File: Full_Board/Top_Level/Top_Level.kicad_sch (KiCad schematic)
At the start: 4 parts, among them J1 OQ0432500000G, J2 OQ0432500000G, J3 OQ0432500000G, J4 OQ0432500000G

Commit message: Fixed entire BOM for all components
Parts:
- J1, J2, J3, J4: Digikey Link https://www.digikey.com/en/products/detail/amphenol-anytek/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 -> (none); Digikey link (none) -> https://www.digikey.com/en/products/detail/amphenol-anytek/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; Manufacturer's Part Number (none) -> OQ0432500000G; Manufacturer_Part_Number OQ0432500000G -> (none); Mouser Price/Stock https://www.mouser.co.uk/ProductDetail/Amphenol-Anytek/OQ04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 -> (none); Mouser link (none) -> https://www.mouser.com/ProductDetail/Amphenol-Anytek/OQ0432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
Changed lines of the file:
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@@
     (company "The Great Gambit")
-  )
-  (bus_entry (at 72.39 186.69) (size 2.54 2.54)
-    (stroke (width 0) (type default) (color 0 0 0 0))
   )
   (wire (pts (xy 68.58 95.25) (xy 68.58 105.41))
@@
       (effects (font (size 1.27 1.27)) (justify left) hide)
     )
-    (property "Mouser Price/Stock" "https://www.mouser.co.uk/ProductDetail/Amphenol-Anytek/OQ0432500000G?qs=Mv7BduZupUhaPicvo3xrhg%3D%3D" (id 7) (at 140.97 109.22 0)
+    (property "Mouser Price/Stock" "" (id 7) (at 140.97 109.22 0)
       (effects (font (size 1.27 1.27)) (justify left) hide)
     )
@@
       (effects (font (size 1.27 1.27)) (justify left) hide)
     )
-    (property "Manufacturer_Part_Number" "OQ0432500000G" (id 9) (at 140.97 114.3 0)
+    (property "Manufacturer_Part_Number" "" (id 9) (at 140.97 114.3 0)
       (effects (font (size 1.27 1.27)) (justify left) hide)
     )
@@
       (effects (font (size 1.27 1.27)) hide)
     )
-    (property "Digikey Link" "https://www.digikey.com/en/products/detail/amphenol-anytek/OQ0432500000G/2261265" (id 11) (at 157.48 99.06 0)
+    (property "Digikey Link" "" (id 11) (at 157.48 99.06 0)
       (effects (font (size 1.27 1.27)) hide)
     )
     (property "Mouser Link" "" (id 12) (at 157.48 99.06 0)
+      (effects (font (size 1.27 1.27)) hide)
+    )
+    (property "Digikey link" "https://www.digikey.com/en/products/detail/amphenol-anytek/OQ0432500000G/2261265" (id 13) (at 157.48 99.06 0)
+      (effects (font (size 1.27 1.27)) hide)
+    )
+    (property "Manufacturer's Part Number" "OQ0432500000G" (id 14) (at 157.48 99.06 0)
+      (effects (font (size 1.27 1.27)) hide)
+    )
+    (property "Mouser link" "https://www.mouser.com/ProductDetail/Amphenol-Anytek/OQ0432500000G?qs=Mv7BduZupUhaPicvo3xrhg%3D%3D" (id 15) (at 157.48 99.06 0)
       (effects (font (size 1.27 1.27)) hide)
     )
@@
       (effects (font (size 1.27 1.27)) (justify left) hide)
     )
-    (property "Mouser Price/Stock" "https://www.mouser.co.uk/ProductDetail/Amphenol-Anytek/OQ0432500000G?qs=Mv7BduZupUhaPicvo3xrhg%3D%3D" (id 7) (at 273.05 121.92 0)
+    (property "Mouser Price/Stock" "" (id 7) (at 273.05 121.92 0)
       (effects (font (size 1.27 1.27)) (justify left) hide)
     )
@@
       (effects (font (size 1.27 1.27)) (justify left) hide)
     )
-    (property "Manufacturer_Part_Number" "OQ0432500000G" (id 9) (at 273.05 127 0)
+    (property "Manufacturer_Part_Number" "" (id 9) (at 273.05 127 0)
       (effects (font (size 1.27 1.27)) (justify left) hide)
     )
@@
       (effects (font (size 1.27 1.27)) hide)
     )
-    (property "Digikey Link" "https://www.digikey.com/en/products/detail/amphenol-anytek/OQ0432500000G/2261265" (id 11) (at 256.54 111.76 0)
+    (property "Digikey Link" "" (id 11) (at 256.54 111.76 0)
       (effects (font (size 1.27 1.27)) hide)
     )
     (property "Mouser Link" "" (id 12) (at 256.54 111.76 0)
+      (effects (font (size 1.27 1.27)) hide)
+    )
+    (property "Digikey link" "https://www.digikey.com/en/products/detail/amphenol-anytek/OQ0432500000G/2261265" (id 13) (at 256.54 111.76 0)
+      (effects (font (size 1.27 1.27)) hide)
+    )
+    (property "Manufacturer's Part Number" "OQ0432500000G" (id 14) (at 256.54 111.76 0)
+      (effects (font (size 1.27 1.27)) hide)
+    )
+    (property "Mouser link" "https://www.mouser.com/ProductDetail/Amphenol-Anytek/OQ0432500000G?qs=Mv7BduZupUhaPicvo3xrhg%3D%3D" (id 15) (at 256.54 111.76 0)
       (effects (font (size 1.27 1.27)) hide)
     )
@@
       (effects (font (size 1.27 1.27)) (justify left) hide)
     )
-    (property "Mouser Price/Stock" "https://www.mouser.co.uk/ProductDetail/Amphenol-Anytek/OQ0432500000G?qs=Mv7BduZupUhaPicvo3xrhg%3D%3D" (id 7) (at 273.05 59.69 0)
+    (property "Mouser Price/Stock" "" (id 7) (at 273.05 59.69 0)
       (effects (font (size 1.27 1.27)) (justify left) hide)
     )
@@
       (effects (font (size 1.27 1.27)) (justify left) hide)
     )
-    (property "Manufacturer_Part_Number" "OQ0432500000G" (id 9) (at 273.05 64.77 0)
+    (property "Manufacturer_Part_Number" "" (id 9) (at 273.05 64.77 0)
       (effects (font (size 1.27 1.27)) (justify left) hide)
     )
@@
       (effects (font (size 1.27 1.27)) hide)
     )
-    (property "Digikey Link" "https://www.digikey.com/en/products/detail/amphenol-anytek/OQ0432500000G/2261265" (id 11) (at 256.54 49.53 0)
+    (property "Digikey Link" "" (id 11) (at 256.54 49.53 0)
       (effects (font (size 1.27 1.27)) hide)
     )
     (property "Mouser Link" "" (id 12) (at 256.54 49.53 0)
+      (effects (font (size 1.27 1.27)) hide)
+    )
+    (property "Digikey link" "https://www.digikey.com/en/products/detail/amphenol-anytek/OQ0432500000G/2261265" (id 13) (at 256.54 49.53 0)
+      (effects (font (size 1.27 1.27)) hide)
+    )
+    (property "Manufacturer's Part Number" "OQ0432500000G" (id 14) (at 256.54 49.53 0)
+      (effects (font (size 1.27 1.27)) hide)
+    )
+    (property "Mouser link" "https://www.mouser.com/ProductDetail/Amphenol-Anytek/OQ0432500000G?qs=Mv7BduZupUhaPicvo3xrhg%3D%3D" (id 15) (at 256.54 49.53 0)
       (effects (font (size 1.27 1.27)) hide)
     )
@@
       (effects (font (size 1.27 1.27)) (justify left) hide)
     )
-    (property "Mouser Price/Stock" "https://www.mouser.co.uk/ProductDetail/Amphenol-Anytek/OQ0432500000G?qs=Mv7BduZupUhaPicvo3xrhg%3D%3D" (id 7) (at 273.05 90.17 0)
+    (property "Mouser Price/Stock" "" (id 7) (at 273.05 90.17 0)
       (effects (font (size 1.27 1.27)) (justify left) hide)
     )
@@
       (effects (font (size 1.27 1.27)) (justify left) hide)
     )
-    (property "Manufacturer_Part_Number" "OQ0432500000G" (id 9) (at 273.05 95.25 0)
+    (property "Manufacturer_Part_Number" "" (id 9) (at 273.05 95.25 0)
       (effects (font (size 1.27 1.27)) (justify left) hide)
     )
@@
       (effects (font (size 1.27 1.27)) hide)
     )
-    (property "Digikey Link" "https://www.digikey.com/en/products/detail/amphenol-anytek/OQ0432500000G/2261265" (id 11) (at 256.54 80.01 0)
+    (property "Digikey Link" "" (id 11) (at 256.54 80.01 0)
       (effects (font (size 1.27 1.27)) hide)
     )
@@
       (effects (font (size 1.27 1.27)) hide)
     )
+    (property "Digikey link" "https://www.digikey.com/en/products/detail/amphenol-anytek/OQ0432500000G/2261265" (id 13) (at 256.54 80.01 0)
+      (effects (font (size 1.27 1.27)) hide)
+    )
+    (property "Manufacturer's Part Number" "OQ0432500000G" (id 14) (at 256.54 80.01 0)
+      (effects (font (size 1.27 1.27)) hide)
+    )
+    (property "Mouser link" "https://www.mouser.com/ProductDetail/Amphenol-Anytek/OQ0432500000G?qs=Mv7BduZupUhaPicvo3xrhg%3D%3D" (id 15) (at 256.54 80.01 0)
+      (effects (font (size 1.27 1.27)) hide)
+    )

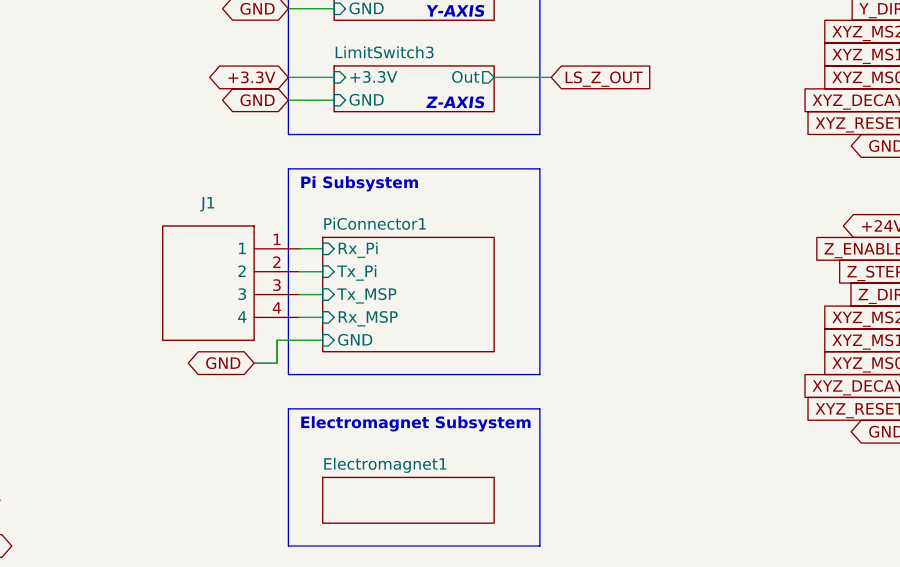
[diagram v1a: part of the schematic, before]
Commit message: Adjusted the Pi subsystem
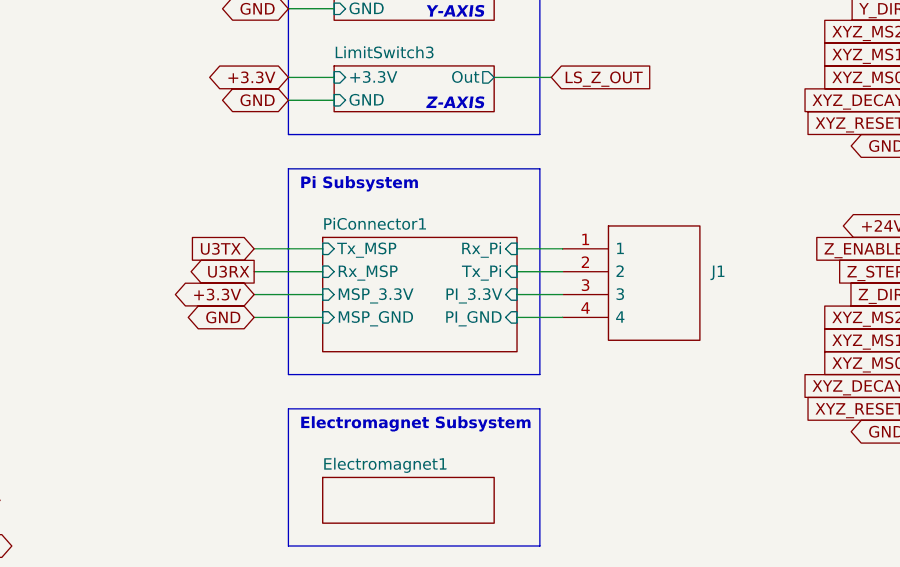
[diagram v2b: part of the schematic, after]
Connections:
- net PiConnector1/Rx_MSP renamed PiConnector1/PI_GND
- net PiConnector1/Tx_MSP renamed PiConnector1/PI_3.3V
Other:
- sheet PiConnector1 ports: added MSP_3.3V, MSP_GND, PI_3.3V, PI_GND; removed GND

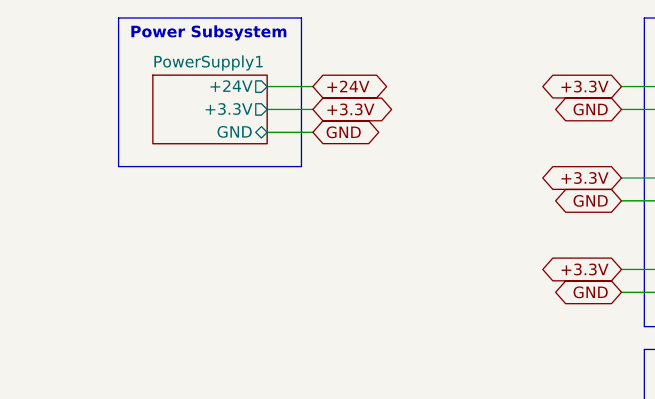
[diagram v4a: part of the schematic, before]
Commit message: Added extra bypass caps to the power supply
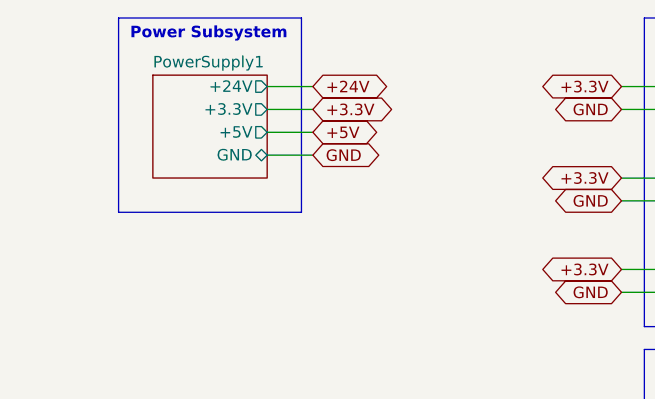
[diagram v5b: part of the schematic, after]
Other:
- sheet PowerSupply1 ports: added +5V; removed none

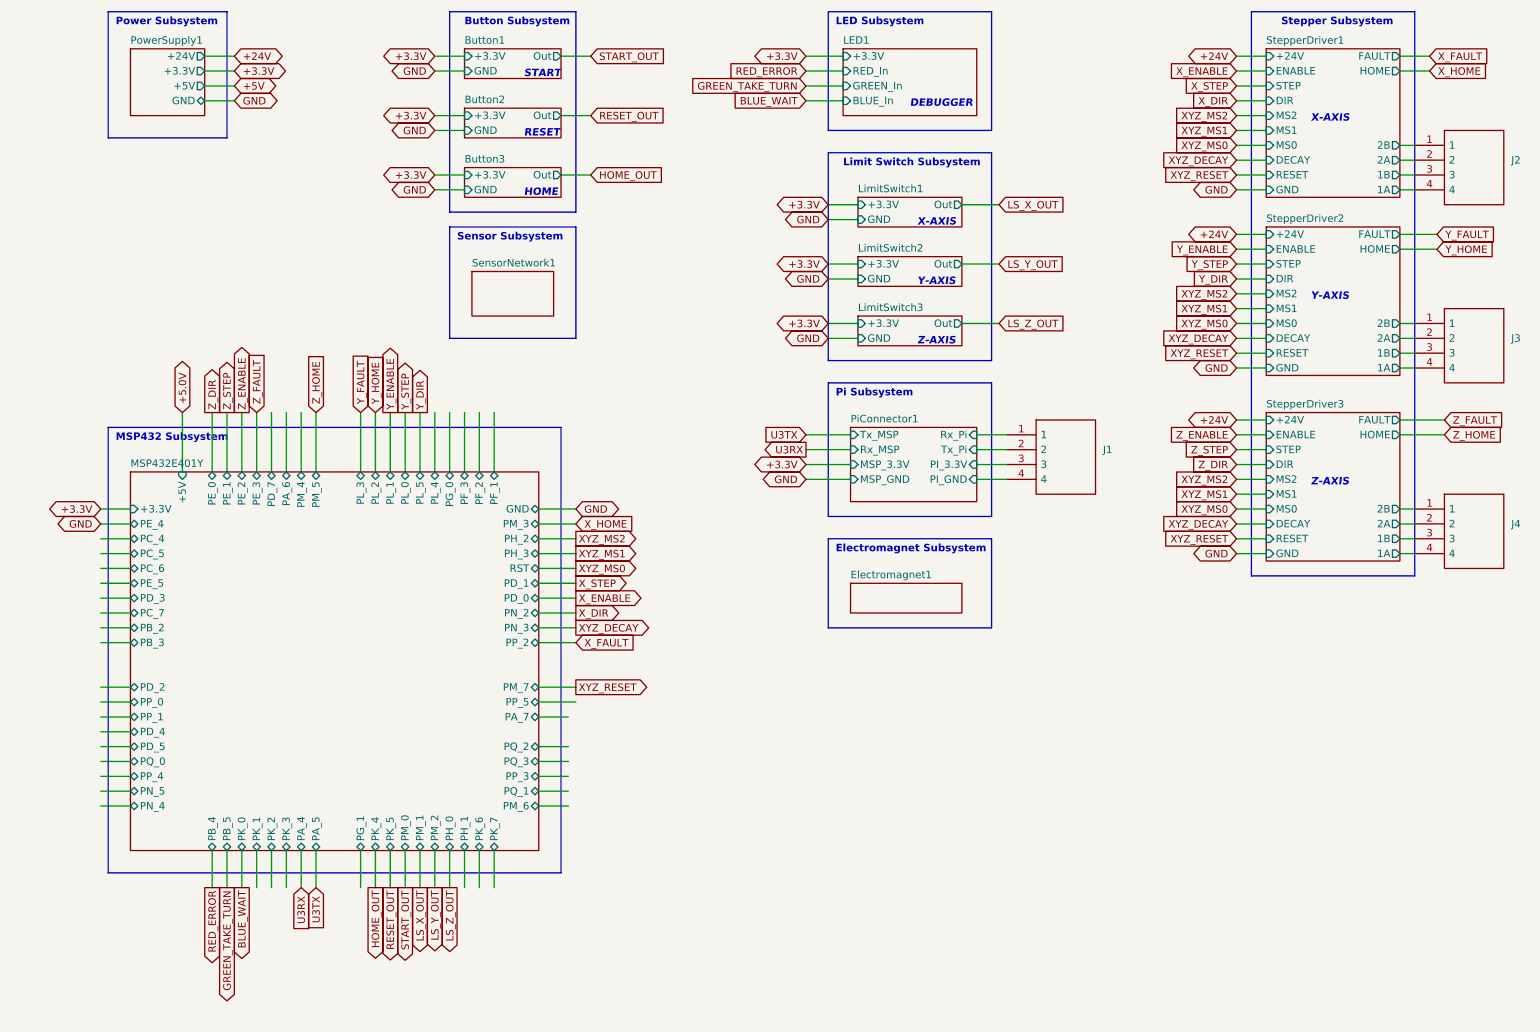
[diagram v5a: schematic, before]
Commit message: Merge Eli and Gabi files. Remove unecessary ECAD remnants. Update stepper components post-part order
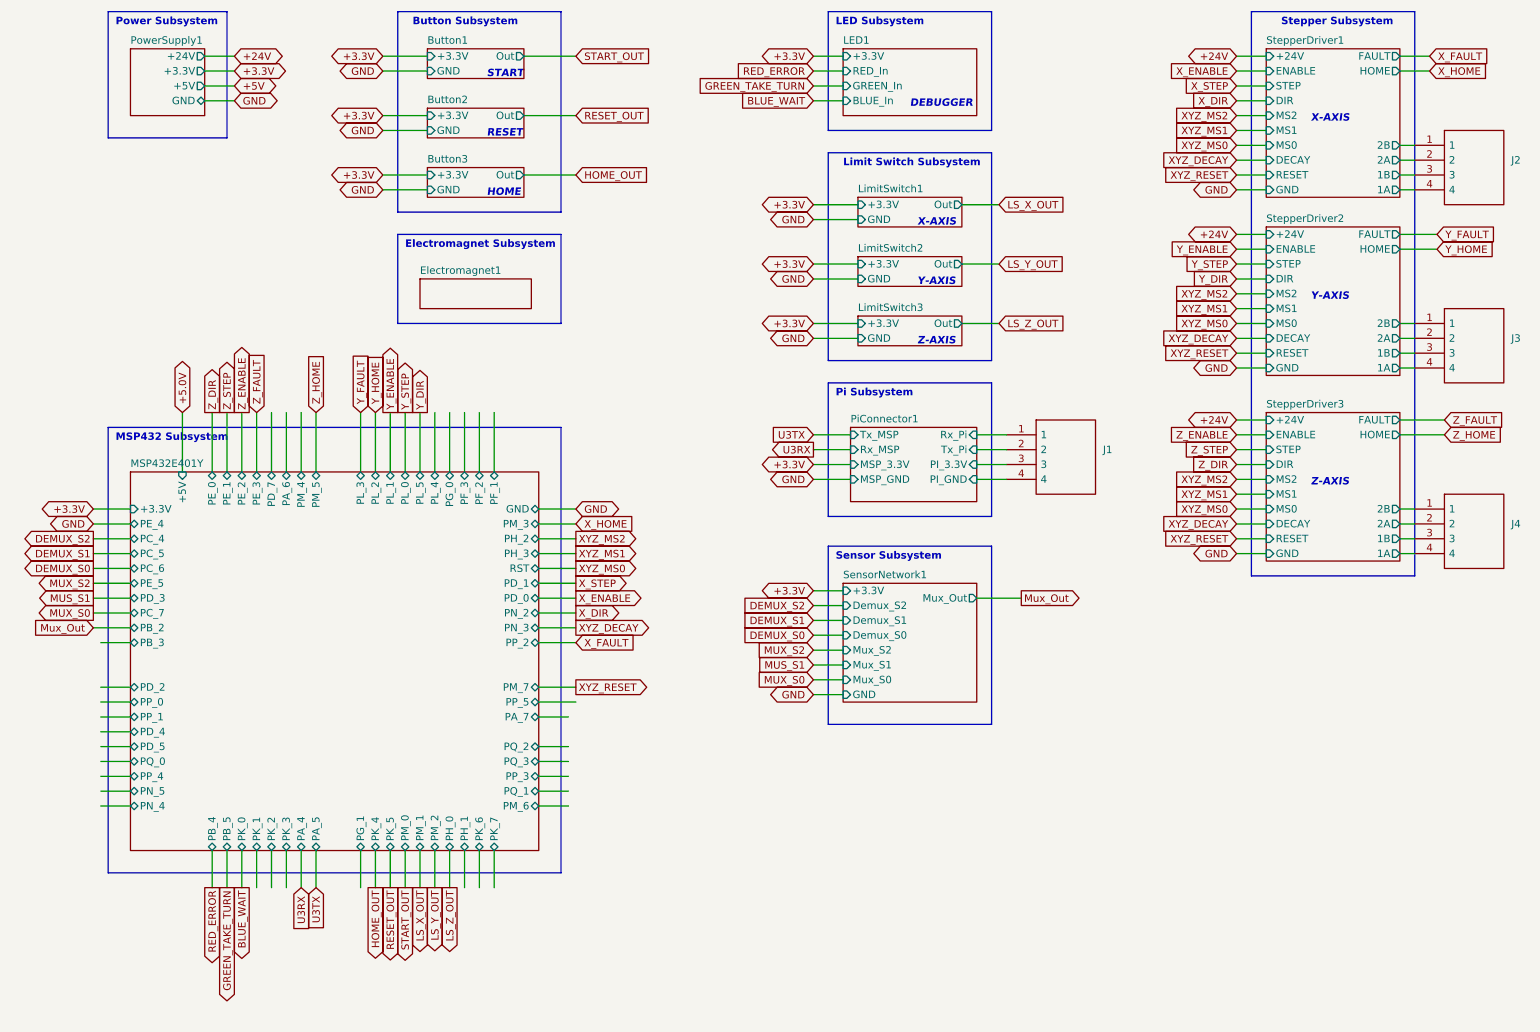
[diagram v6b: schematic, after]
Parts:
- J1, J2, J3, J4: Digikey Link (none) -> https://www.digikey.com/en/products/detail/amphenol-anytek/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; Manufacturer_Part_Number (none) -> OQ0432500000G; Mouser Price/Stock (none) -> https://www.mouser.co.uk/ProductDetail/Amphenol-Anytek/OQ04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
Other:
- sheet SensorNetwork1 ports: added +3.3V, Demux_S0, Demux_S1, Demux_S2, GND, Mux_Out, Mux_S0, Mux_S1, Mux_S2; removed none

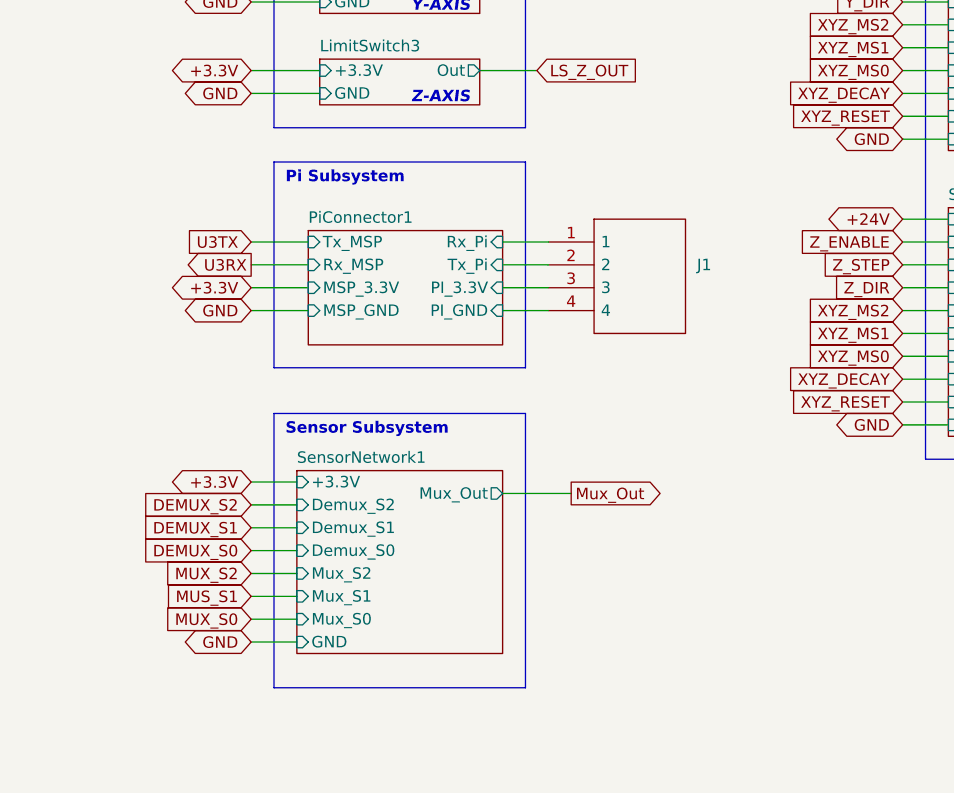
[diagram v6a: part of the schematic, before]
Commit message: Added a fuse and fixed ERC
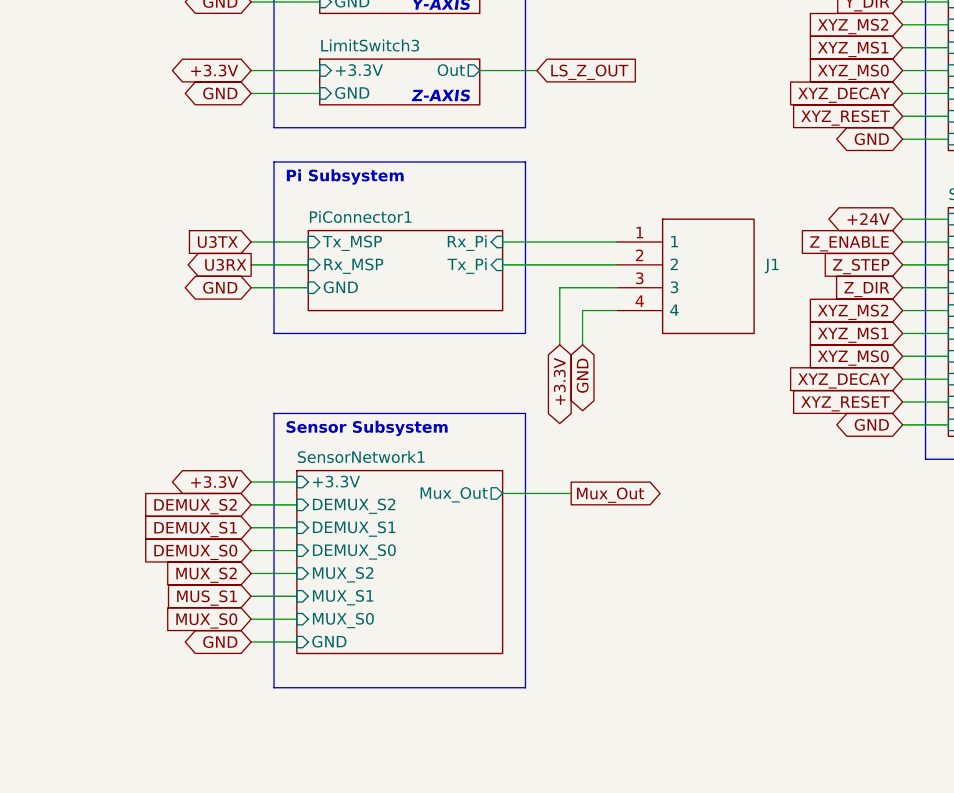
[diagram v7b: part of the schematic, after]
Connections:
- net PiConnector1/PI_3.3V is gone; now on net +3.3V: J1.3
- net PiConnector1/PI_GND is gone; now on net GND: J1.4
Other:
- sheet PiConnector1 ports: added GND; removed MSP_3.3V, MSP_GND, PI_3.3V, PI_GND
- sheet SensorNetwork1 ports: added DEMUX_S0, DEMUX_S1, DEMUX_S2, MUX_S0, MUX_S1, MUX_S2; removed Demux_S0, Demux_S1, Demux_S2, Mux_S0, Mux_S1, Mux_S2
- moved on the sheet: J1
